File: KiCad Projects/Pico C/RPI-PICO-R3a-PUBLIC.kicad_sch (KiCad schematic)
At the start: 38 parts, among them J3 USB_C_Receptacle_USB2.0_16P, J4 SM03B-SRSS-TB, Q1 DMG1012T-7, SW1 PTS810 SJM 250 SMTR LFSPTS810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, U2 RT6150B-33GQW, U3 W25Q16JVUXIQ, Y1 ECS-120-8-33-JGN-TR

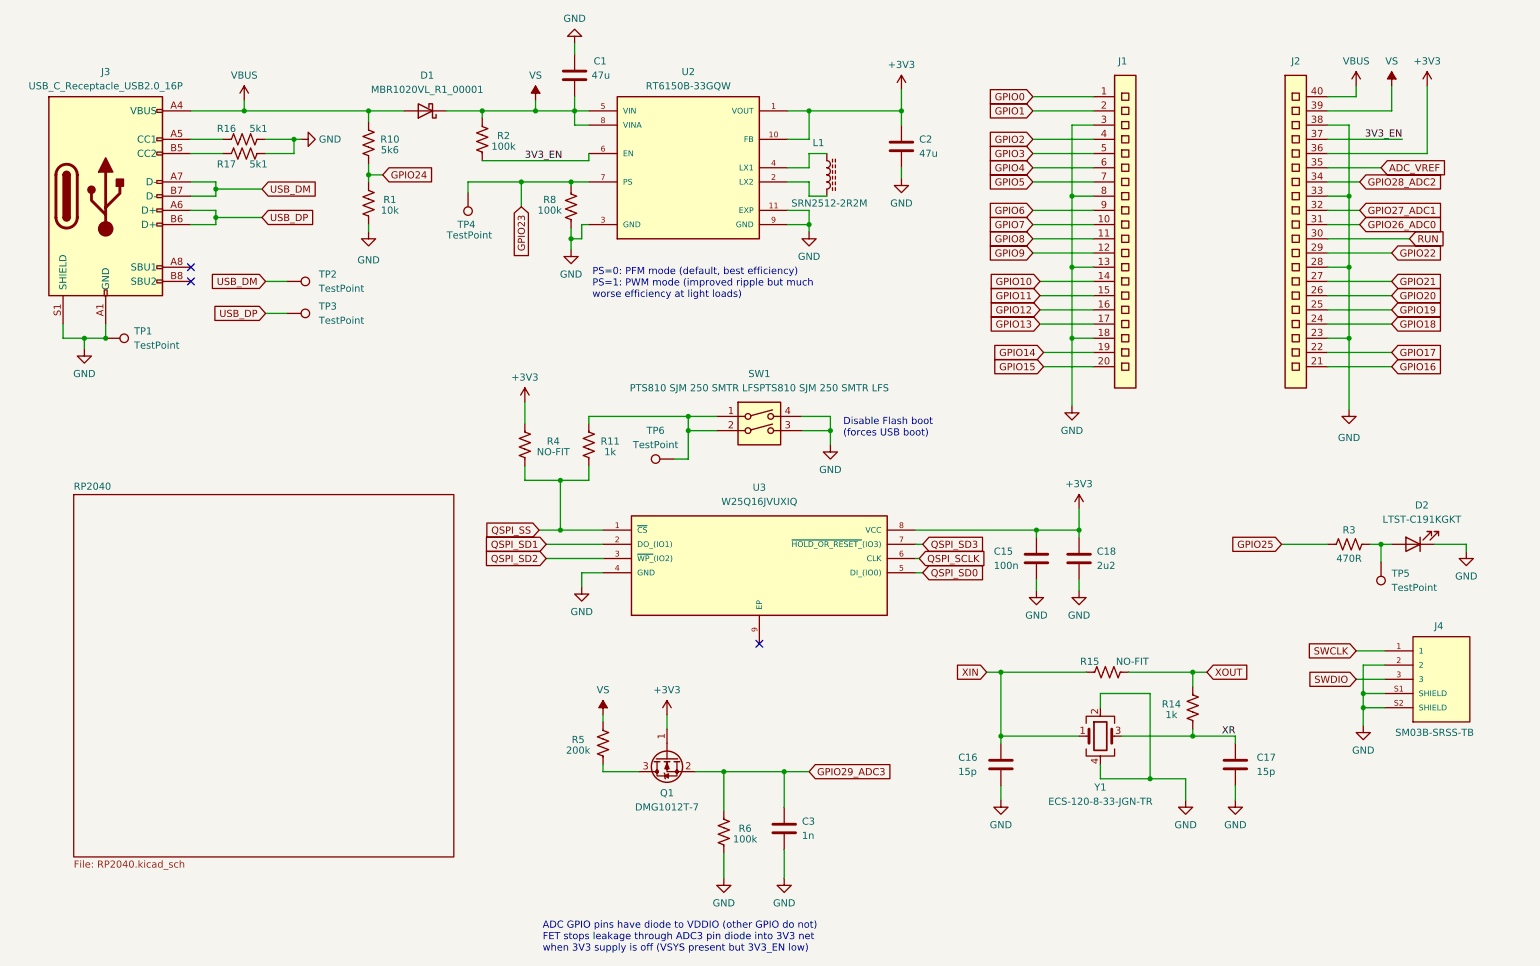
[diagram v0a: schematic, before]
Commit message: Added Pico 2
Added an initial design for the Pico 2. Also updated the original Pico C to v4 (without README update since I'm waiting on boards to ship).
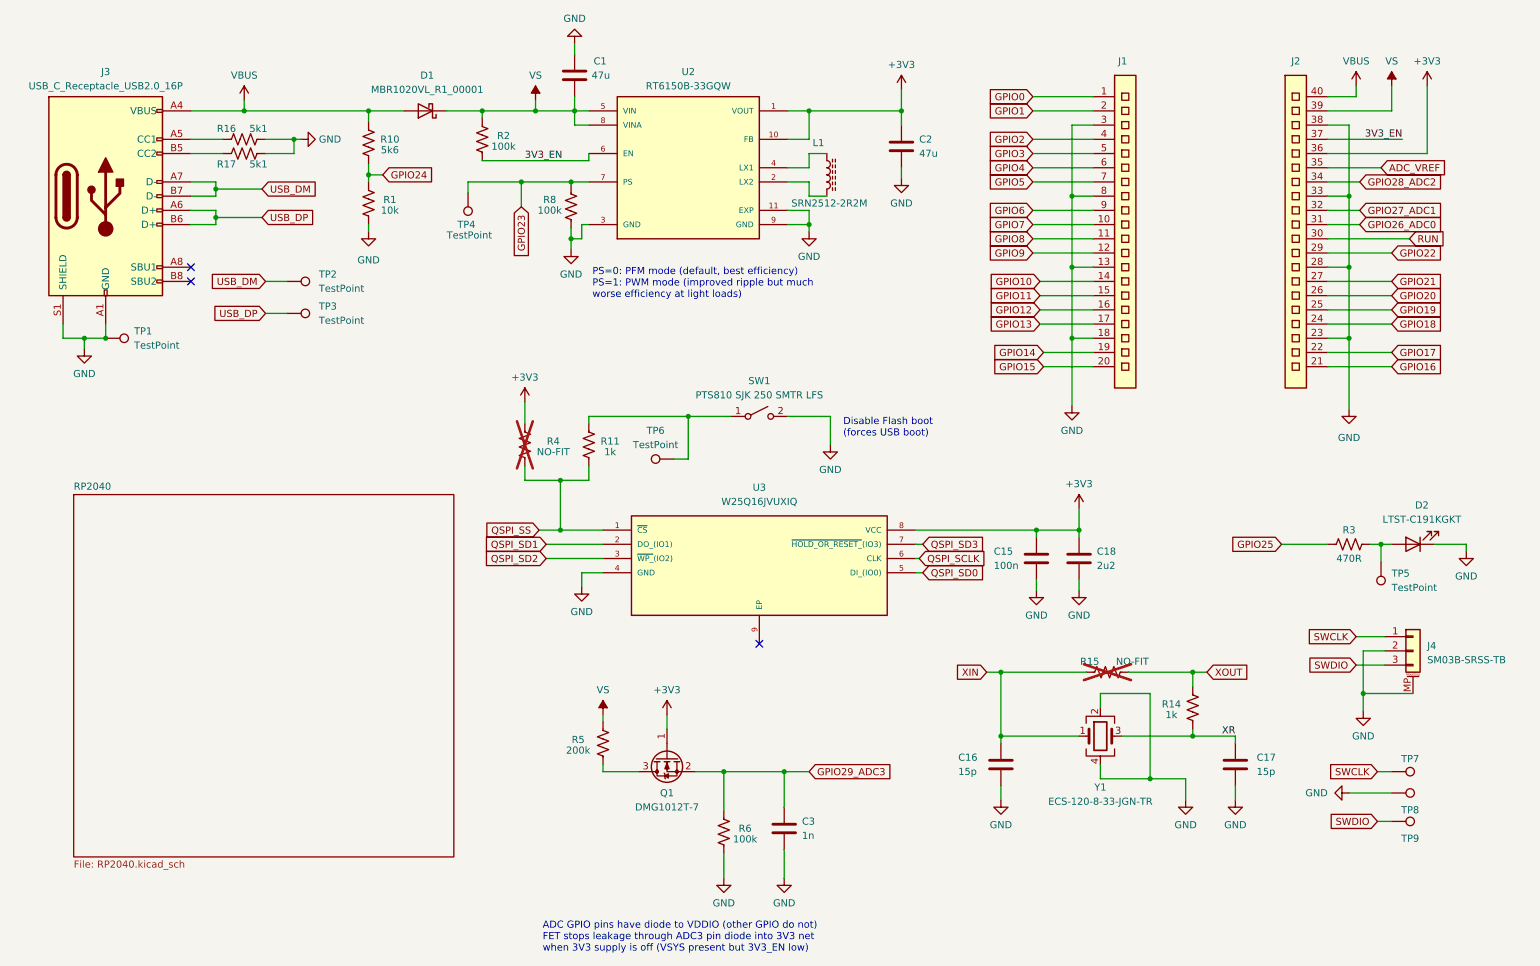
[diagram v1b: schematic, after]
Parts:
- removed J4: SM03B-SRSS-TB, Pico_C:JST_SM03B-SRSS-TB_LF__SN_, symbol Pico_C:SM03B-SRSS-TB_LF__SN_
- removed SW1: PTS810 SJM 250 SMTR LFSPTS810 SJM 250 SMTR LFS, Pico_C:SW_SPST_PTS810, symbol Switch:SW_DIP_x02
- added J4: SM03B-SRSS-TB, Connector_JST:JST_SH_SM03B-SRSS-TB_1x03-1MP_P1.00mm_Horizontal, symbol Connector_Generic_MountingPin:Conn_01x03_MountingPin
- added SW1: PTS810 SJK 250 SMTR LFS, Button_Switch_SMD:SW_SPST_PTS810, symbol Switch:SW_SPST
- added TP7, TP8, TP9: TestPoint, TestPoint:TestPoint_Pad_1.5x1.5mm, symbol Connector:TestPoint
- C15, C16, C17, C3: footprint Pico_C:C_0201_0603Metric -> Capacitor_SMD:C_0201_0603Metric
- D1: footprint Pico_C:DIOM3616X98N -> Diode_SMD:D_SOD-123F
- Q1: footprint Pico_C:SOT50P160X90-3N -> Package_TO_SOT_SMD:SOT-523
- R15, R4: now not fitted
- U2: footprint Pico_C:SON50P250X250X80-11N -> Package_DFN_QFN:DFN-10-1EP_2.6x2.6mm_P0.5mm_EP1.3x2.2mm
- Y1: footprint Pico_C:XTAL_ECS-120-8-33-JGN-TR -> Crystal:Crystal_SMD_SeikoEpson_FA238-4Pin_3.2x2.5mm
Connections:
- net GND: now also J4.2 (Pin_2), J4.MP (MountPin), SW1.2 (B), TP8.1
- net SWCLK: now also J4.1 (Pin_1), TP7.1
- net SWDIO: now also J4.3 (Pin_3), TP9.1
- net at R11.2, TP6.1: now also SW1.1 (A)
